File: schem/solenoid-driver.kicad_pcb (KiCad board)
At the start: 2 copper layers, 42 x 17 mm, 25 parts, among them J1 Conn_01x03, J2 SOLENOID, Q1 AO3400, U1 MIC2009A-1, U3 MIC2250-2

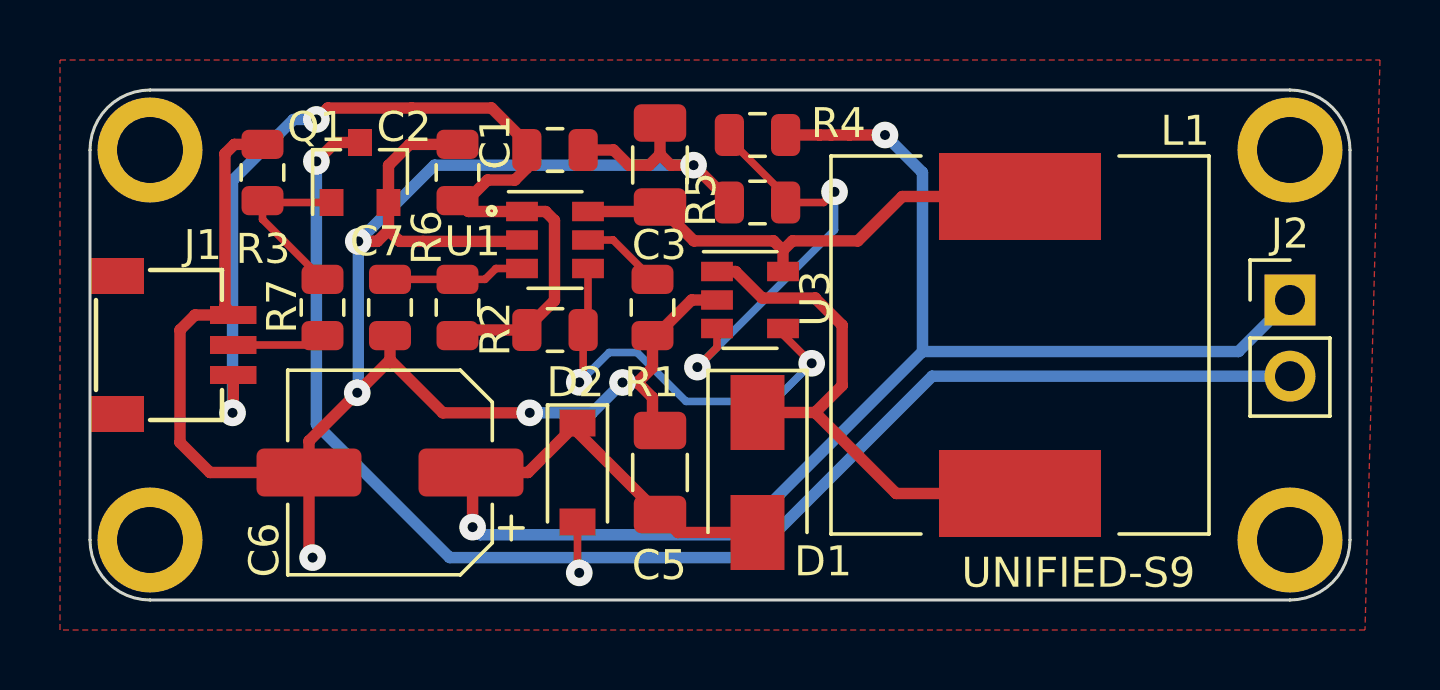
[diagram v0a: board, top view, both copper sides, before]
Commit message: Fix pinout and regenerate gerber
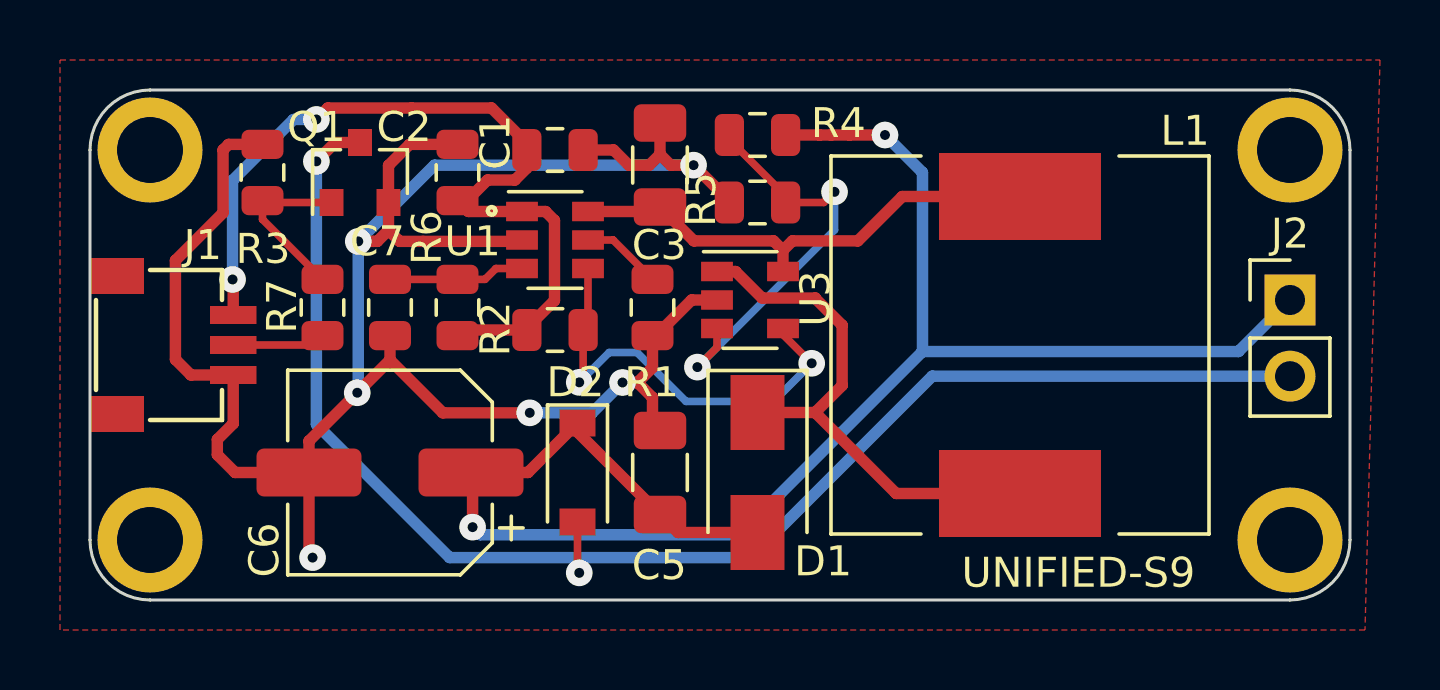
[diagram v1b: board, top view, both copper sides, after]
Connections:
- J1 pad 1: GND -> +5V
- J1 pad 3: +5V -> GND
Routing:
- net +5V: track 33.9 -> 29.3 mm
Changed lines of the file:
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@@
     (thickness 1.6)
     (drawings 15)
-    (tracks 177)
+    (tracks 180)
     (zones 0)
     (modules 25)
@@
       (drillshape 0)
       (scaleselection 1)
-      (outputdirectory "Gerbers/"))
+      (outputdirectory "Gerber"))
   )
   (net 0 "")
@@
   (module random-keyboard-parts:JST-SR-3 (layer F.Cu)
     (at 170 117.5 270)
+    (attr smd)
     (fp_text reference J1 (at -3.327 -3.759 180) (layer F.SilkS)
       (effects (font (size 1 1) (thickness 0.15)))
@@
     (fp_line (start -2.5 -4.4) (end -1.5 -4.4) (layer F.SilkS) (width 0.15))
     (pad 3 smd rect (at 1 -4.775 270) (size 0.6 1.55) (layers F.Cu F.Paste F.Mask)
-      (net 2 +5V))
+      (net 1 GND))
     (pad 2 smd rect (at 0 -4.775 270) (size 0.6 1.55) (layers F.Cu F.Paste F.Mask)
       (net 10 SIGNAL))
     (pad 1 smd rect (at -1 -4.775 270) (size 0.6 1.55) (layers F.Cu F.Paste F.Mask)
-      (net 1 GND))
+      (net 2 +5V))
     (pad "" smd rect (at -2.3 -0.9 270) (size 1.2 1.8) (layers F.Cu F.Paste F.Mask))
     (pad "" smd rect (at 2.3 -0.9 270) (size 1.2 1.8) (layers F.Cu F.Paste F.Mask))
@@
   (segment (start 188.643 111.506) (end 187.96 111.506) (width 0.381) (layer F.Cu) (net 1))
   (via (at 178.943 114.046) (size 0.889) (drill 0.3302) (layers F.Cu B.Cu) (net 1))
-  (segment (start 174.8105 110.8125) (end 175.75 110.8125) (width 0.381) (layer F.Cu) (net 1))
-  (segment (start 174.498 111.125) (end 174.8105 110.8125) (width 0.381) (layer F.Cu) (net 1))
-  (segment (start 174.775 116.5) (end 174.498 116.223) (width 0.381) (layer F.Cu) (net 1))
-  (segment (start 174.498 116.223) (end 174.498 111.125) (width 0.381) (layer F.Cu) (net 1))
   (segment (start 182.25 110.8125) (end 180.6525 110.8125) (width 0.381) (layer F.Cu) (net 1))
   (segment (start 179.95 111.515) (end 179.95 112.75) (width 0.381) (layer F.Cu) (net 1))
@@
   (segment (start 177.3 121.75) (end 177.3 120.7) (width 0.381) (layer F.Cu) (net 1))
   (segment (start 180 118) (end 180 117.1875) (width 0.381) (layer F.Cu) (net 1))
-  (segment (start 177.3 121.75) (end 174 121.75) (width 0.381) (layer F.Cu) (net 1))
-  (segment (start 174 121.75) (end 173 120.75) (width 0.381) (layer F.Cu) (net 1))
-  (segment (start 173 120.75) (end 173 117) (width 0.381) (layer F.Cu) (net 1))
-  (segment (start 173.5 116.5) (end 174.775 116.5) (width 0.381) (layer F.Cu) (net 1))
-  (segment (start 173 117) (end 173.5 116.5) (width 0.381) (layer F.Cu) (net 1))
   (via (at 187.75 118.75) (size 0.889) (drill 0.3302) (layers F.Cu B.Cu) (net 1))
   (segment (start 188.25 118.75) (end 188.75 119.25) (width 0.381) (layer F.Cu) (net 1))
@@
   (segment (start 181.761 119.761) (end 180 118) (width 0.381) (layer F.Cu) (net 1))
   (segment (start 184.658 119.761) (end 181.761 119.761) (width 0.381) (layer F.Cu) (net 1))
+  (segment (start 177.3 121.75) (end 174.836 121.75) (width 0.381) (layer F.Cu) (net 1))
+  (segment (start 174.836 121.75) (end 174.244 121.158) (width 0.381) (layer F.Cu) (net 1))
+  (segment (start 174.244 121.158) (end 174.244 120.65) (width 0.381) (layer F.Cu) (net 1))
+  (segment (start 174.775 120.119) (end 174.775 118.5) (width 0.381) (layer F.Cu) (net 1))
+  (segment (start 174.244 120.65) (end 174.775 120.119) (width 0.381) (layer F.Cu) (net 1))
+  (segment (start 173.364 118.5) (end 172.847 117.983) (width 0.381) (layer F.Cu) (net 1))
+  (segment (start 174.775 118.5) (end 173.364 118.5) (width 0.381) (layer F.Cu) (net 1))
+  (segment (start 172.847 117.983) (end 172.847 114.681) (width 0.381) (layer F.Cu) (net 1))
+  (segment (start 172.847 114.681) (end 174.4345 113.0935) (width 0.381) (layer F.Cu) (net 1))
+  (segment (start 174.62 110.8125) (end 175.75 110.8125) (width 0.381) (layer F.Cu) (net 1))
+  (segment (start 174.4345 113.0935) (end 174.4345 110.998) (width 0.381) (layer F.Cu) (net 1))
+  (segment (start 174.4345 110.998) (end 174.62 110.8125) (width 0.381) (layer F.Cu) (net 1))
   (segment (start 182.6125 113.05) (end 182.25 112.6875) (width 0.381) (layer F.Cu) (net 2))
   (segment (start 184.4 113.05) (end 182.6125 113.05) (width 0.381) (layer F.Cu) (net 2))
@@
   (segment (start 180.721 109.601) (end 177.927 109.601) (width 0.381) (layer F.Cu) (net 2))
   (segment (start 177.927 109.601) (end 177.546 109.982) (width 0.381) (layer F.Cu) (net 2))
-  (via (at 174.752 119.761) (size 0.889) (drill 0.3302) (layers F.Cu B.Cu) (net 2))
-  (segment (start 174.775 118.5) (end 174.775 119.738) (width 0.381) (layer F.Cu) (net 2))
-  (segment (start 174.775 119.738) (end 174.752 119.761) (width 0.381) (layer F.Cu) (net 2))
   (segment (start 176.784 109.982) (end 177.546 109.982) (width 0.381) (layer B.Cu) (net 2))
-  (segment (start 174.752 119.761) (end 174.752 112.014) (width 0.381) (layer B.Cu) (net 2))
   (segment (start 174.752 112.014) (end 176.784 109.982) (width 0.381) (layer B.Cu) (net 2))
+  (via (at 174.752 115.316) (size 0.889) (drill 0.3302) (layers F.Cu B.Cu) (net 2))
+  (segment (start 174.775 115.339) (end 174.752 115.316) (width 0.381) (layer F.Cu) (net 2))
+  (segment (start 174.775 116.5) (end 174.775 115.339) (width 0.381) (layer F.Cu) (net 2))
+  (segment (start 174.752 115.316) (end 174.752 112.014) (width 0.381) (layer B.Cu) (net 2))
   (segment (start 188.85 113.05) (end 189 112.9) (width 0.381) (layer F.Cu) (net 3))
   (segment (start 186.6 113.05) (end 188.85 113.05) (width 0.381) (layer F.Cu) (net 3))

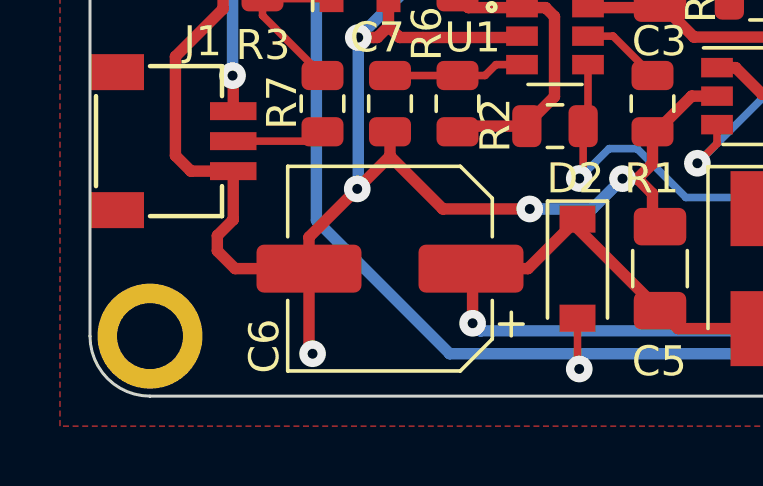
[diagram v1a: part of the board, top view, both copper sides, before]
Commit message: Remove an unnecessary via
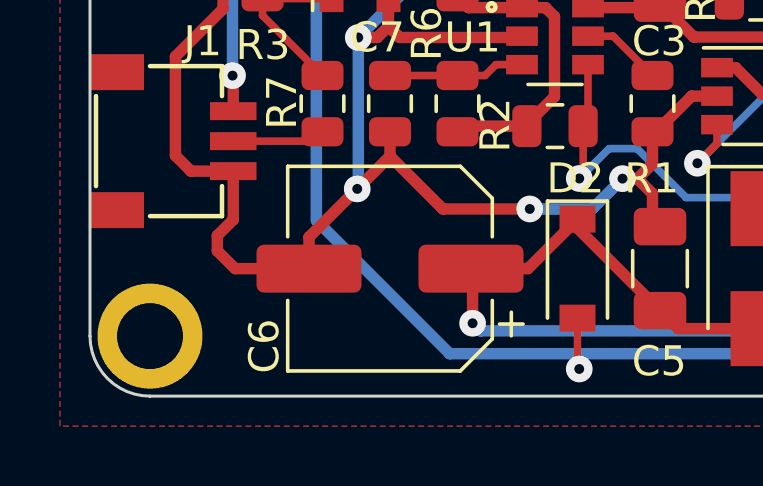
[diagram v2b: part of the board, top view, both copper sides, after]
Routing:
- net GND: track 76.7 -> 73.8 mm, vias 6 -> 5
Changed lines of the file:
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@@
     (thickness 1.6)
     (drawings 15)
-    (tracks 180)
+    (tracks 177)
     (zones 0)
     (modules 25)
@@
   (segment (start 188.75 118.25) (end 188.25 118.75) (width 0.381) (layer F.Cu) (net 1))
   (segment (start 188.75 117.1875) (end 188.75 118.25) (width 0.381) (layer F.Cu) (net 1))
-  (via (at 177.419 124.587) (size 0.889) (drill 0.3302) (layers F.Cu B.Cu) (net 1))
-  (segment (start 177.3 121.75) (end 177.3 124.468) (width 0.381) (layer F.Cu) (net 1))
-  (segment (start 177.3 124.468) (end 177.419 124.587) (width 0.381) (layer F.Cu) (net 1))
   (via (at 178.9085 119.0915) (size 0.889) (drill 0.3302) (layers F.Cu B.Cu) (net 1))
   (segment (start 178.943 119.057) (end 178.9085 119.0915) (width 0.381) (layer B.Cu) (net 1))
